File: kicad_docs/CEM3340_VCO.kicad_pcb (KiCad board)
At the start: 2 copper layers, 55.9 x 78.7 mm, 96 parts, among them J1 tuning controls, J2 1 v/oct inputs, J3 linear FM input, J4 sync input, J5 PWM inputs, J6 power input, Q1 MMDT3904, U1 L78L10_SOT89, U2 MC7905, U3 REF02AU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

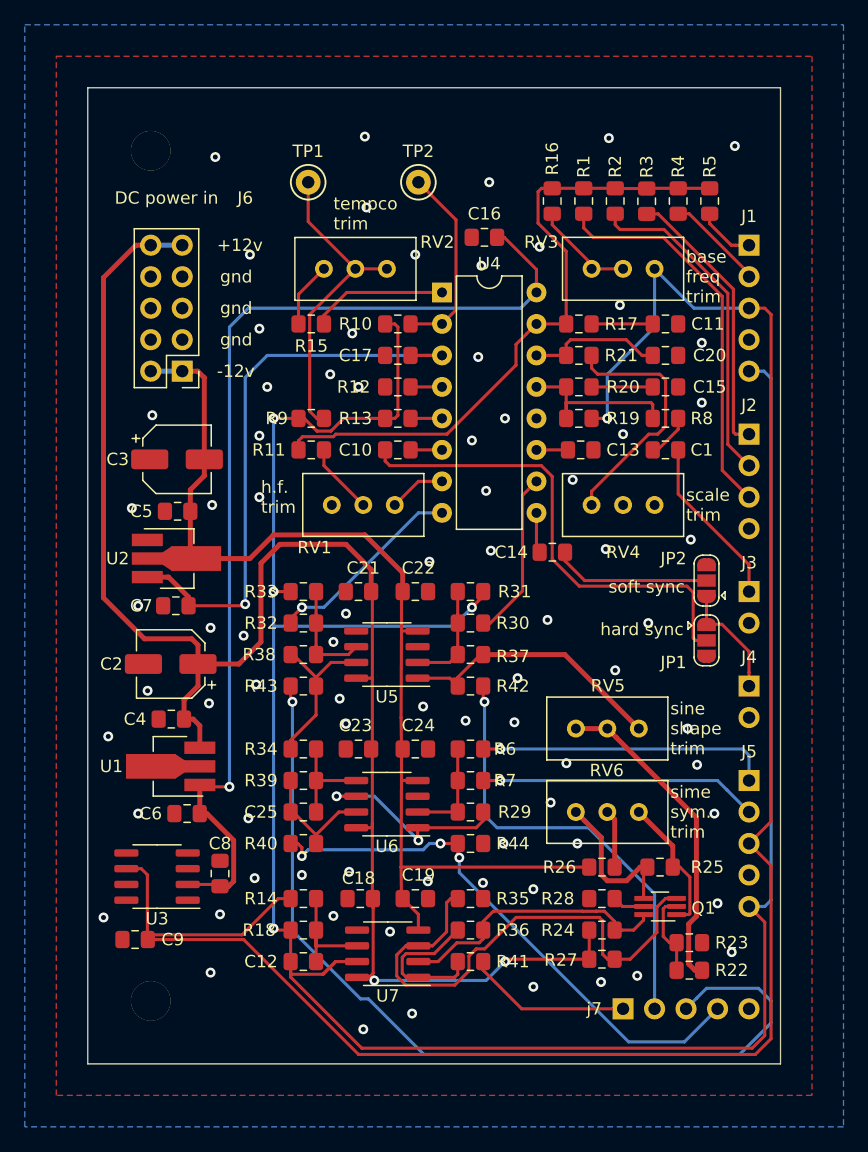
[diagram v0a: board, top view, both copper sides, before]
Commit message: extract circuit blocks into separate schem pages
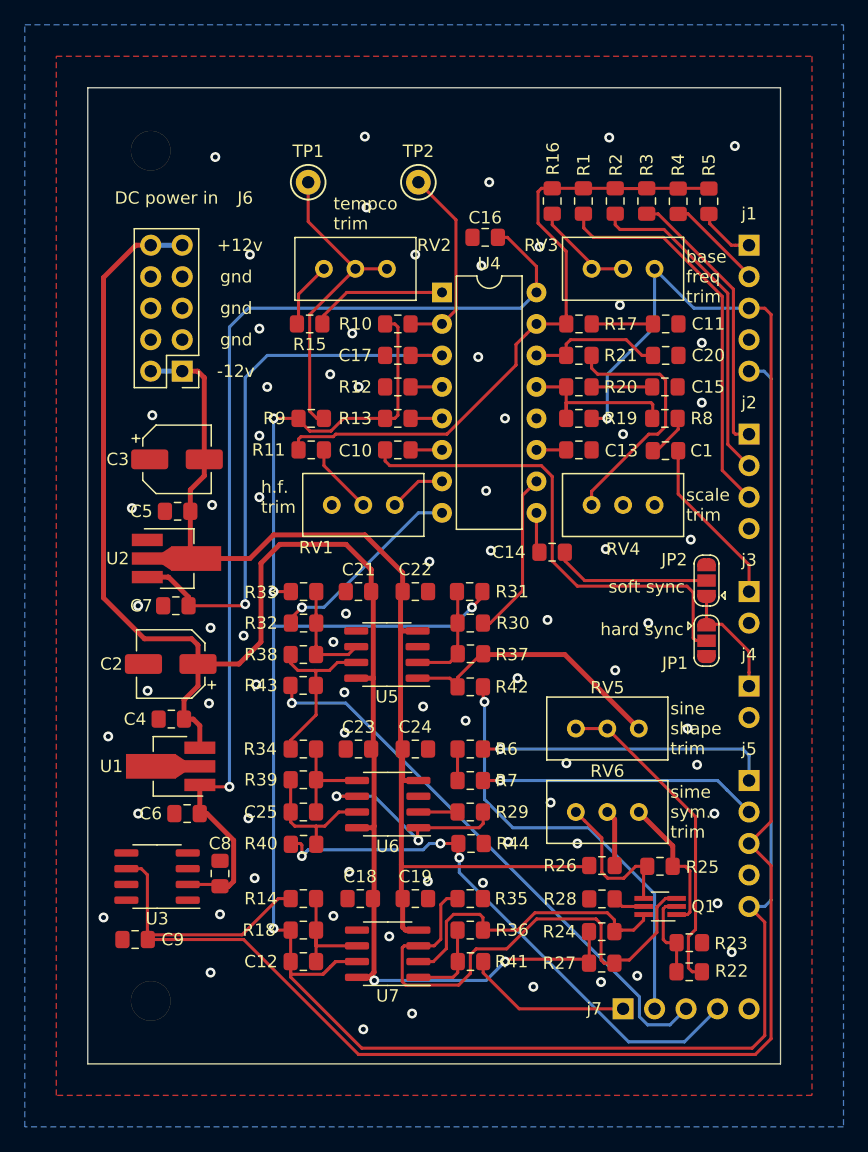
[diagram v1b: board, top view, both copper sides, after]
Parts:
- R30: value 39k -> ???
- R32: value 82k -> ???
- moved R27 0.32 mm to (117.7, 121.4)
- moved C13 0.14 mm to (115.8, 80.0)
- moved R24 0.13 mm to (117.7, 118.9)
- moved R22 0.13 mm to (124.7, 122.1)
- moved R26 0.13 mm to (117.7, 113.5)
- moved R15 0.13 mm to (94.1, 69.8)
- moved R42 0.07 mm to (107.1, 99.1)
- moved R40 0.07 mm to (93.6, 111.8)
- moved R5 0.07 mm to (126.3, 60.0)
- moved U6 0.06 mm to (100.4, 108.6)
- moved R25 0.06 mm to (122.4, 113.6)
- moved C16 0.06 mm to (108.3, 62.9)
- moved R39 0.06 mm to (93.6, 106.6)
- moved C1 0.06 mm to (122.8, 80.1)
- moved R31 0.06 mm to (107.0, 91.4)
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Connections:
- net 10_vpp_saw renamed Net-(R34-Pad2)
- net 10_vpp_tri renamed Net-(R37-Pad1)
- net buffered_pulse_out renamed /Waveshapers/10vpp_pulse_v_out
- net buffered_saw_out renamed /Waveshapers/10vpp_saw_v_out
- net buffered_sine_out renamed /Waveshapers/10vpp_sine_v_out
- net buffered_tri_out renamed /Waveshapers/10vpp_triangle_v_out
- net expo_fm_summing_node renamed /Signal_Inputs/expo_cv_i_out
- net hard_sync_in renamed /VCO_Core/hard_sync_v_in
- net lin_fm_summing_node renamed /Signal_Inputs/lin_cv_i_out
- net raw_saw renamed /Waveshapers/raw_saw_v_in
- net raw_triangle renamed /Waveshapers/raw_triangle_v_in
- net soft_sync_in renamed /VCO_Core/soft_sync_v_in
- R29 pad 2: pwm_cv_summing_node -> Net-(R29-Pad2)
- R6 pad 1: pwm_cv_summing_node -> /Signal_Inputs/pulse_width_i_out
- R7 pad 1: pwm_cv_summing_node -> /Signal_Inputs/pulse_width_i_out
- U6 pad 2: pwm_cv_summing_node -> Net-(R29-Pad2)
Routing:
- net /Waveshapers/10vpp_saw_v_out: track 73.3 -> 45.6 mm
- net pwm_cv_summing_node: track 8.32 -> 0.00 mm
- net Net-(R36-Pad1): track 12.4 -> 6.77 mm
- net -15V: track 89.7 -> 93.3 mm
- net Net-(R29-Pad2): track 0.00 -> 2.72 mm
- net /Signal_Inputs/pulse_width_i_out: track 0.00 -> 2.54 mm
- net Net-(Q1-Pad6): track 22.5 -> 24.7 mm
- net /Waveshapers/10vpp_triangle_v_out: track 36.1 -> 35.3 mm
- net Net-(C25-Pad1): track 10.1 -> 10.8 mm
- net GND: vias 78 -> 73
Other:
- board text added: "github.com/JordanAceto/CEM3340_VCO rev 1 01/29/2020"
- board text removed: "github.com/JordanAceto/CEM3340_VCO rev 0 01/29/2020"

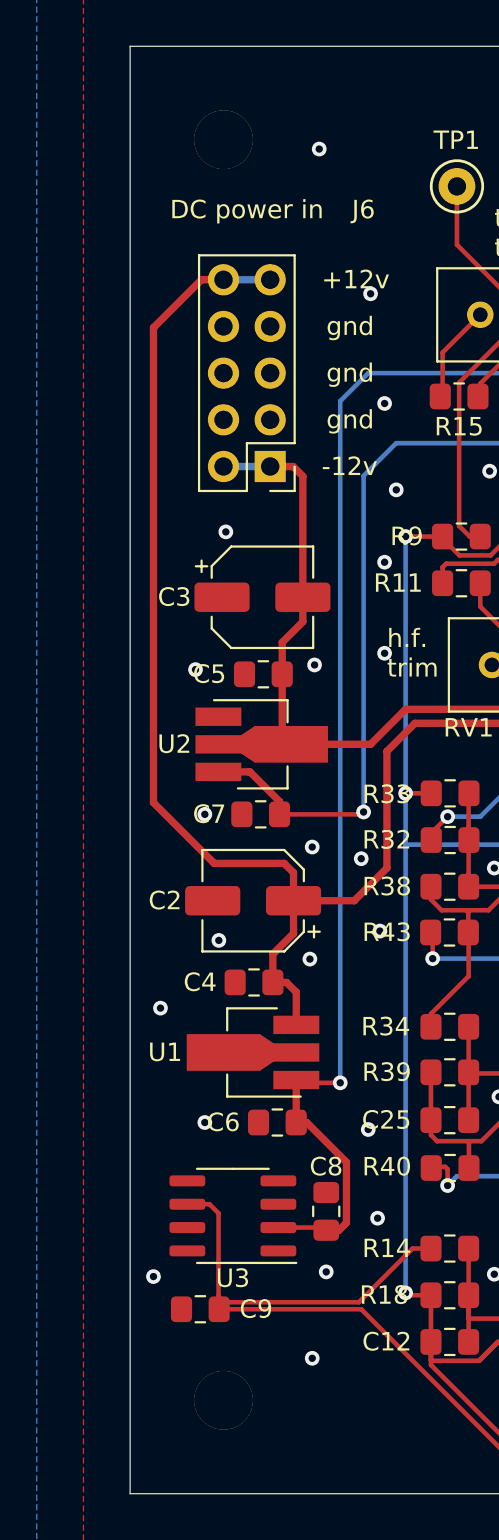
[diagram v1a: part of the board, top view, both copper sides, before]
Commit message: finalize some values, update documentation
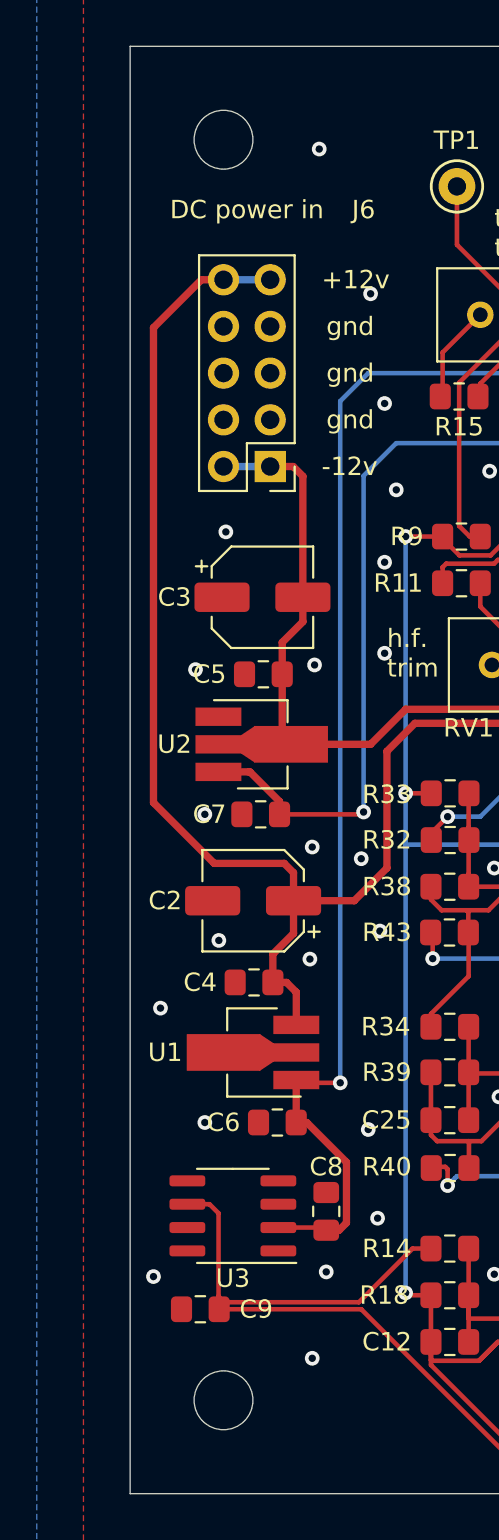
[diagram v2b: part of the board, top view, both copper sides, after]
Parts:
- removed hole 1: MountingHole_3.2mm_M3, MountingHole:MountingHole_3.2mm_M3
- removed hole 2: MountingHole_3.2mm_M3, MountingHole:MountingHole_3.2mm_M3
- added H1: MountingHole, MountingHole:MountingHole_3.2mm_M3, F.Cu at (81.3, 55.9)
- added H2: MountingHole, MountingHole:MountingHole_3.2mm_M3, F.Cu at (81.3, 124.5)
- C12: value C -> 100nF
- R30: value ??? -> 34k
- R32: value ??? -> 68k
- R35, R36: value 11k -> 15k
- R4: value ??? -> 1M
- R40, R44: value R -> 2k
- R5: value ??? -> 100k
- R6: value 270k -> 110k
